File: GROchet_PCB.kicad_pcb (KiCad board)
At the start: 2 copper layers, 100 x 58 mm, 102 parts, among them J1 Conn_01x04_Pin, J10 Conn_01x04_Pin, J11 Conn_01x03_Pin, J12 Conn_01x04_Pin, J13 Conn_01x02_Pin, J14 Conn_01x02_Pin, J15 Conn_01x02_Pin, J16 Conn_01x02_Pin, J17 Conn_01x02_Pin, J18 Conn_01x02_Pin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

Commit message: finished routing
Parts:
- removed C20, C21, C22: 1uF, Capacitor_SMD:C_0603_1608Metric_Pad1.08x0.95mm_HandSolder
- removed D10, D11, D9: 1N4148W, Diode_SMD:D_SOD-123
- removed J16, J17, J18: Conn_01x02_Pin, Connector_JST:JST_EH_B2B-EH-A_1x02_P2.50mm_Vertical
- removed R28, R32, R33: 1k, Resistor_SMD:R_0603_1608Metric_Pad0.98x0.95mm_HandSolder
- removed R29, R30, R31: 10k, Resistor_SMD:R_0603_1608Metric_Pad0.98x0.95mm_HandSolder
- R22, R25: value 10k -> 1k
- R23, R24: value 1k -> 10k
- moved D1 80.4 mm to (202.9, 69.8), turned to 90 degrees
- moved D2 76.7 mm to (207.9, 69.8), turned to 90 degrees
- moved D3 73.3 mm to (212.9, 69.8), turned to 90 degrees
- moved D4 70.2 mm to (217.9, 69.8), turned to 90 degrees
- moved R24 69.0 mm to (214.5, 54.9), turned to -90 degrees
- moved D5 67.6 mm to (222.9, 69.8), turned to 90 degrees
- moved R22 66.3 mm to (217.9, 59.7)
- moved R17 65.5 mm to (213.1, 58.9), turned to 180 degrees
- moved C17 59.0 mm to (221.2, 61.2), turned to 180 degrees
- moved R21 58.2 mm to (221.2, 59.7), turned to 180 degrees
- moved D6 57.3 mm to (217.2, 57.8), turned to 180 degrees
- moved R25 57.0 mm to (226.5, 60.2), turned to 90 degrees
- moved R23 55.0 mm to (228.9, 59.7), turned to 180 degrees
- moved J13 52.0 mm to (218.5, 64.0), turned to 0 degrees
- moved C18 51.0 mm to (228.9, 61.1), turned to 180 degrees
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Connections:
- A1 pad D36: /X_MIN -> /Z_MIN
- A1 pad D37: /X_MAX -> unconnected-(A1-PadD37)
- A1 pad D39: /Y_MAX -> unconnected-(A1-PadD39)
- A1 pad D40: /Z_MIN -> /X_MIN
- A1 pad D41: /Z_MAX -> unconnected-(A1-PadD41)
- C17 pad 2: /X_MAX -> /X_MIN
- C18 pad 2: /X_MIN -> /Y_MIN
- C19 pad 2: /Y_MAX -> /Z_MIN
- D6 pad 1: /X_MAX -> /X_MIN
- D7 pad 1: /X_MIN -> /Y_MIN
- D8 pad 1: /Y_MAX -> /Z_MIN
- R21 pad 2: /X_MAX -> /X_MIN
- R22 pad 1: +5V -> Net-(J13-Pin_1)
- R23 pad 1: Net-(J18-Pin_1) -> +5V
- R23 pad 2: /X_MAX -> /Y_MIN
- R24 pad 1: Net-(J13-Pin_1) -> +5V
- R24 pad 2: /X_MIN -> /LIMIT_INT
- R25 pad 1: +5V -> Net-(J14-Pin_1)
- R25 pad 2: /Y_MAX -> /Y_MIN
- R26 pad 2: /Y_MIN -> /Z_MIN
- R27 pad 1: Net-(J14-Pin_1) -> Net-(J15-Pin_1)
- R27 pad 2: /Y_MAX -> /Z_MIN
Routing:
- net /DOWN_BTN: track 2.97 -> 156.1 mm, vias 0 -> 1
- net /LEFT_BTN: track 2.97 -> 154.2 mm, vias 0 -> 2
- net /RIGHT_BTN: track 2.97 -> 114.7 mm, vias 0 -> 4
- net /CONF_BTN: track 2.99 -> 110.9 mm, vias 0 -> 3
- net /UP_BTN: track 2.97 -> 83.9 mm, vias 0 -> 2
- net +5V: track 268.2 -> 321.2 mm, vias 3 -> 10
- net /BTN_INT: track 0.00 -> 39.3 mm
- net /X_MIN: track 0.00 -> 37.1 mm, vias 0 -> 1
- net /Y_MIN: track 0.00 -> 35.9 mm, vias 0 -> 1
- net /LIMIT_INT: track 0.00 -> 28.6 mm
- net /Z_MIN: track 0.00 -> 25.2 mm, vias 0 -> 1
- net GND: track 0.00 -> 7.42 mm, vias 4 -> 247
- net /LED_DATA: track 16.7 -> 10.7 mm
- net Net-(J13-Pin_1): track 0.00 -> 4.97 mm
- net Net-(J5-Pin_2): track 12.1 -> 7.61 mm
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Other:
- board size 100 x 58 mm -> 100 x 56 mm

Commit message: aaaaaaaaaaaaaaaaaa
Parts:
- added C20: 10uF, Capacitor_SMD:C_0805_2012Metric, F.Cu at (190.0, 69.8)
- added C21: 10uF, Capacitor_SMD:C_0805_2012Metric, F.Cu at (190.0, 71.8)
- added C22: 470uF, Capacitor_THT:CP_Radial_D8.0mm_P3.50mm, F.Cu at (165.9, 93.8)
- added C26: 470uF, Capacitor_THT:CP_Radial_D8.0mm_P3.50mm, F.Cu at (170.5, 98.7)
- C25: value 100uF -> 10uF; footprint Capacitor_SMD:C_1206_3216Metric -> Capacitor_SMD:C_0805_2012Metric
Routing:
- net Net-(J5-Pin_2): track 7.61 -> 14.1 mm
- net +12V: track 150.3 -> 156.2 mm
- net +5V: track 321.2 -> 323.1 mm
- net GND: vias 247 -> 242
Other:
- board text added: "ARCADE BTNS"
- board text added: "CNF"
- board text added: "DN"
- board text added: "L"
- board text added: "LED1"
- board text added: "LED2"
- board text added: "LIMIT SW"
- board text added: "R"
- board text added: "SERVO"
- board text added: "SW_X"
- board text added: "SW_Y"
- board text added: "SW_Z"
- board text added: "UP"
- board text added: "X_STEPPER"
- board text added: "Y_STEPPER"
- board text added: "Z_STEPPER"

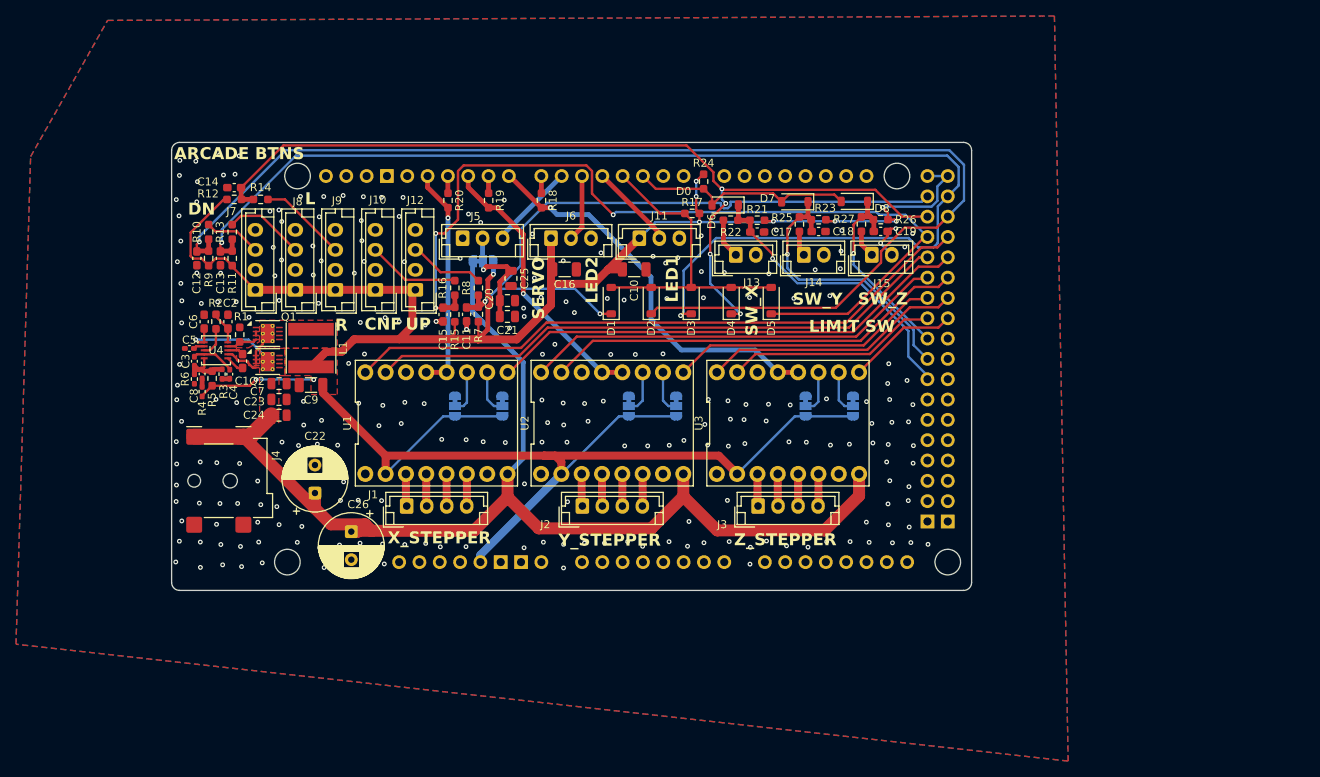
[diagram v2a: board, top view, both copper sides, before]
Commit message: DXL Buffer circuit and new prod file
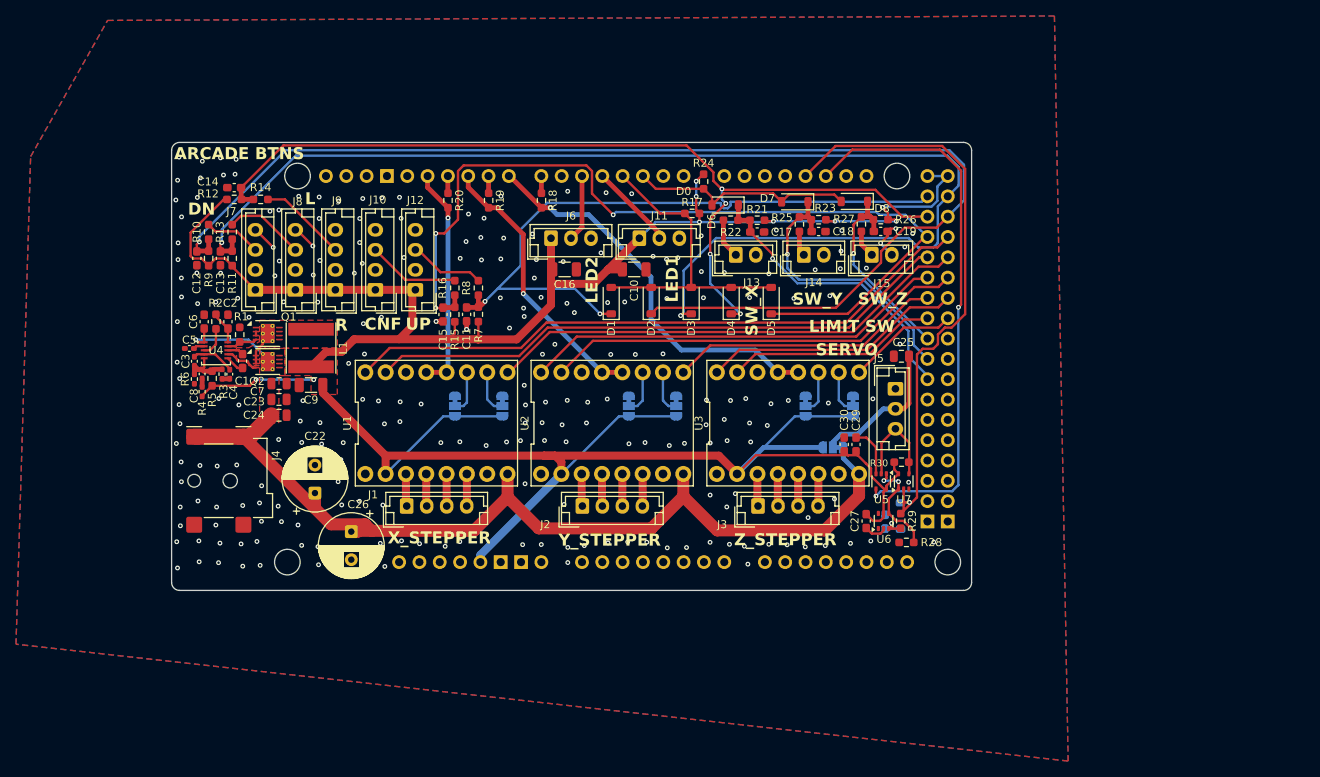
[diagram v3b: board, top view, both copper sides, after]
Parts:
- removed C20, C21: 10uF, Capacitor_SMD:C_0805_2012Metric
- added C27: 100nF, Capacitor_SMD:C_0603_1608Metric_Pad1.08x0.95mm_HandSolder, F.Cu at (234.8, 97.3)
- added C28: 150pF, Capacitor_SMD:C_0603_1608Metric_Pad1.08x0.95mm_HandSolder, B.Cu at (237.2, 97.4)
- added C29: 100nF, Capacitor_SMD:C_0603_1608Metric_Pad1.08x0.95mm_HandSolder, F.Cu at (233.6, 87.8)
- added C30: 100nF, Capacitor_SMD:C_0603_1608Metric_Pad1.08x0.95mm_HandSolder, F.Cu at (232.1, 87.8)
- added D9: D, Diode_SMD:D_SOD-123, B.Cu at (239.1, 96.7)
- added R28: 10k, Resistor_SMD:R_0603_1608Metric_Pad0.98x0.95mm_HandSolder, F.Cu at (239.9, 100.0)
- added R29: 0, Resistor_SMD:R_0603_1608Metric_Pad0.98x0.95mm_HandSolder, F.Cu at (239.1, 97.3)
- added R30: 10k, Resistor_SMD:R_0603_1608Metric_Pad0.98x0.95mm_HandSolder, F.Cu at (239.2, 90.0)
- added U5: 74LVC1G125, Package_TO_SOT_SMD:SOT-353_SC-70-5, F.Cu at (236.7, 92.4)
- added U6: 74HC2G14GW, Package_TO_SOT_SMD:SOT-363_SC-70-6, F.Cu at (237.0, 97.3)
- added U7: 74LVC1G126, Package_TO_SOT_SMD:SOT-353_SC-70-5, F.Cu at (239.5, 92.4)
- moved J5 57.3 mm to (238.5, 80.8), turned to -90 degrees
- moved C25 49.8 mm to (239.2, 76.7), turned to 180 degrees
- moved JP7 49.5 mm to (230.7, 88.1), turned to 180 degrees
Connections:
- A1 pad D18: unconnected-(A1-D18/TX1-PadD18) -> /TTL_TXD
- A1 pad D19: unconnected-(A1-D19/RX1-PadD19) -> /TTL_RXD
- A1 pad D6: /SERVO_DATA -> unconnected-(A1-PadD6)
- J5 pad 3: /SERVO_DATA -> /Limit Switches/DXL_TTL
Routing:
- net /TTL_TXD: track 0.00 -> 75.5 mm, vias 0 -> 1
- net /TTL_RXD: track 0.00 -> 70.6 mm, vias 0 -> 2
- net +5V: track 323.1 -> 358.1 mm, vias 10 -> 9
- net +12V: track 156.2 -> 130.3 mm
- net GND: track 7.42 -> 22.8 mm, vias 242 -> 231
- net /Limit Switches/TTL_TXEN: track 0.00 -> 12.8 mm, vias 0 -> 2
- net /Limit Switches/DXL_TTL: track 0.00 -> 12.7 mm
- net /SERVO_DATA: track 10.8 -> 0.00 mm
- net Net-(D9-A): track 0.00 -> 5.01 mm, vias 0 -> 1
- net Net-(J5-Pin_2): track 14.1 -> 18.1 mm, vias 1 -> 0
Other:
- board text added: "0"
- board text added: "12"
- board text added: "5"
